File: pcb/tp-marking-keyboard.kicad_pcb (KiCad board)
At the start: 2 copper layers, 119 x 77.5 mm, 69 parts, among them J1 Conn_01x02_Socket, Q1 2N7002, SW1 SW_Push, SW10 SW_Push, SW11 SW_Push, SW12 SW_Push, SW13 SW_Push, SW14 SW_Push, SW15 SW_Push, SW16 SW_Push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

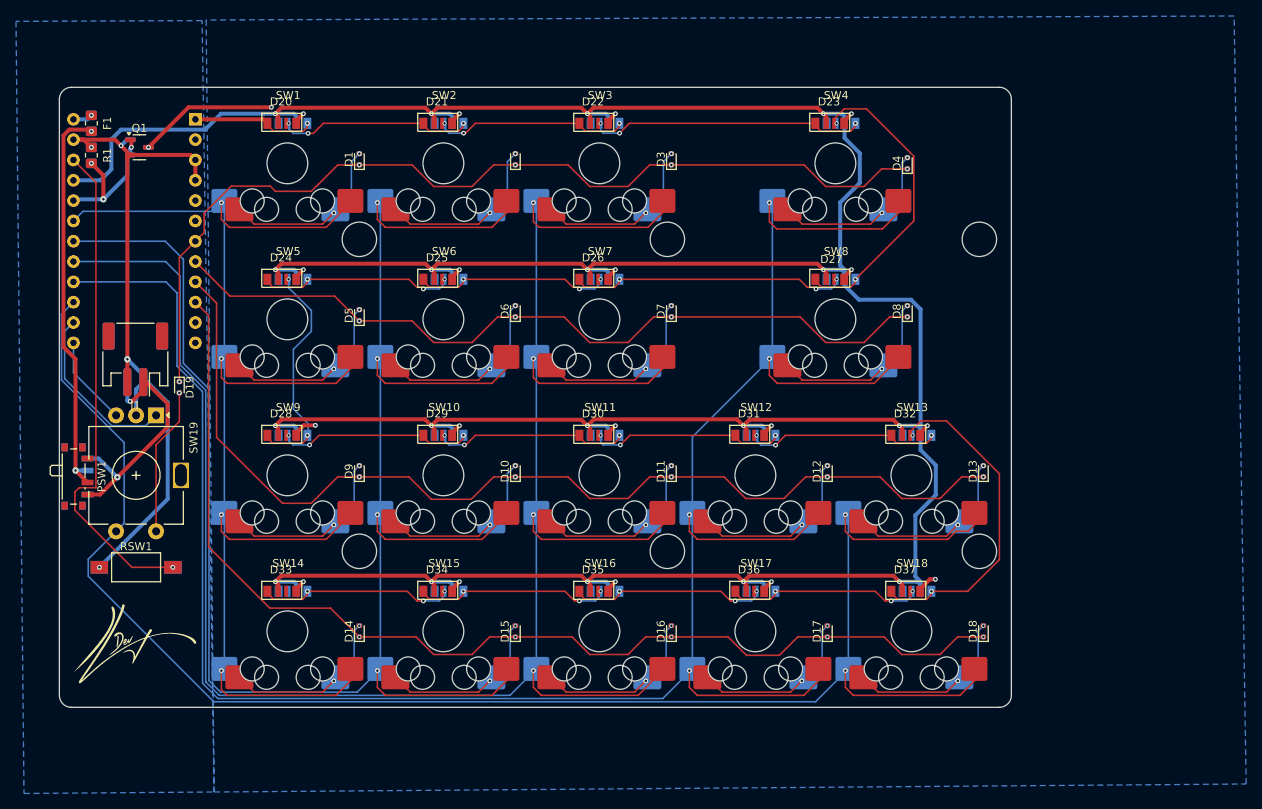
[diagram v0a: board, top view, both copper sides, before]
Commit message: Move led footprints lower
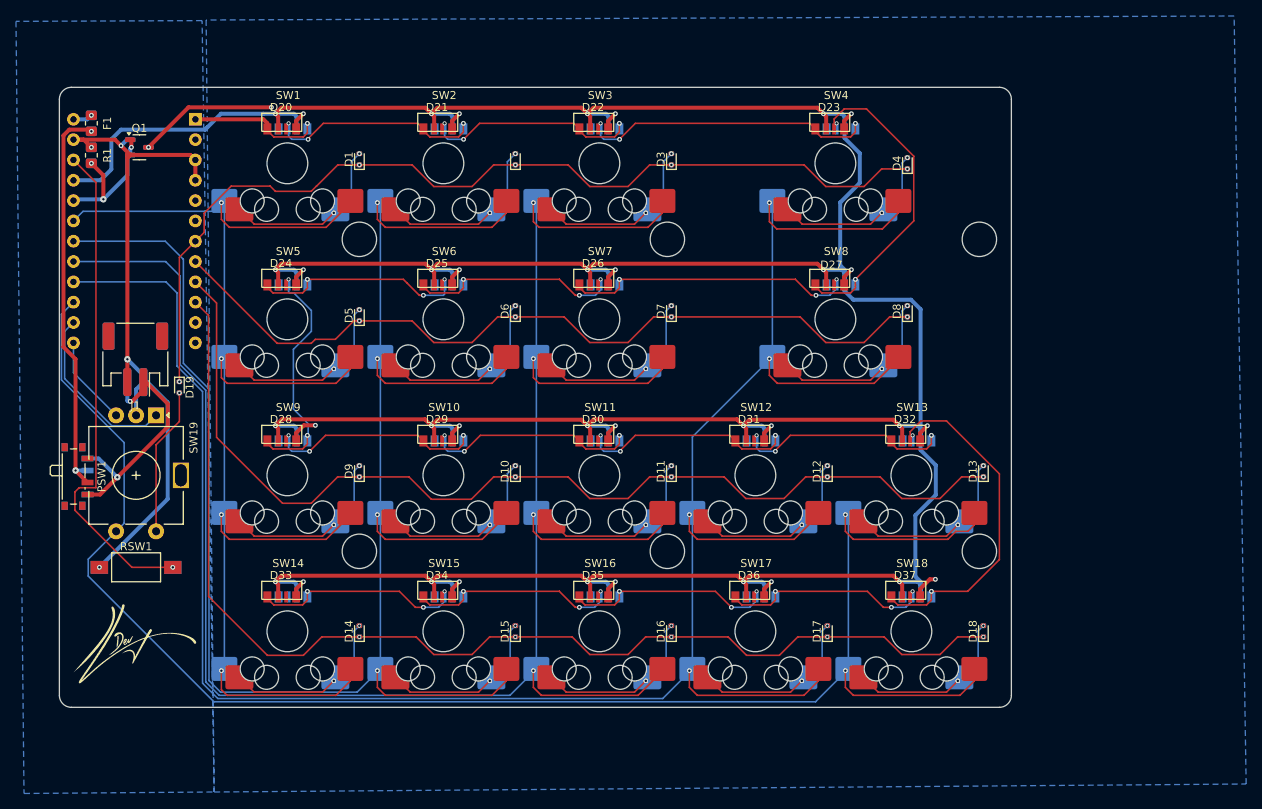
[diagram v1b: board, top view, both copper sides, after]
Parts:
- moved D20 0.70 mm to (89.2, 34.0)
- moved D21 0.70 mm to (108.7, 34.0)
- moved D22 0.70 mm to (128.2, 34.0)
- moved D23 0.70 mm to (157.7, 34.0)
- moved D24 0.70 mm to (89.2, 53.5)
- moved D25 0.70 mm to (108.7, 53.5)
- moved D26 0.70 mm to (128.2, 53.5)
- moved D27 0.70 mm to (157.7, 53.5)
- moved D28 0.70 mm to (89.2, 73.0)
- moved D29 0.70 mm to (108.7, 73.0)
- moved D30 0.70 mm to (128.2, 73.0)
- moved D31 0.70 mm to (147.7, 73.0)
- moved D32 0.70 mm to (167.2, 73.0)
- moved D33 0.70 mm to (89.2, 92.5)
- moved D34 0.70 mm to (108.7, 92.5)
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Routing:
- net VCC: track 492.9 -> 518.5 mm
- net LED_GND: track 48.4 -> 61.0 mm
- net row3: track 140.2 -> 145.7 mm
- net row1: track 99.8 -> 102.1 mm
- net Net-(D32-DOUT): track 42.1 -> 44.2 mm
- net Net-(D29-DOUT): track 24.4 -> 26.2 mm
- net Net-(D31-DOUT): track 24.5 -> 26.0 mm
- net Net-(D20-DOUT): track 24.5 -> 26.0 mm
- net Net-(D28-DOUT): track 24.4 -> 25.9 mm
- net Net-(D24-DIN): track 24.7 -> 26.2 mm
- net Net-(D21-DOUT): track 24.4 -> 25.9 mm
- net Net-(D30-DOUT): track 24.6 -> 26.0 mm
- net LED_DATA: track 15.4 -> 16.8 mm
- net Net-(D23-DOUT): track 38.1 -> 39.5 mm
- net Net-(D22-DOUT): track 34.6 -> 36.0 mm
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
